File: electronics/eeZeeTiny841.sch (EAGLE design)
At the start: 12 parts, among them IC1 ATtiny841, J2 avrisp, Q1 16MHz

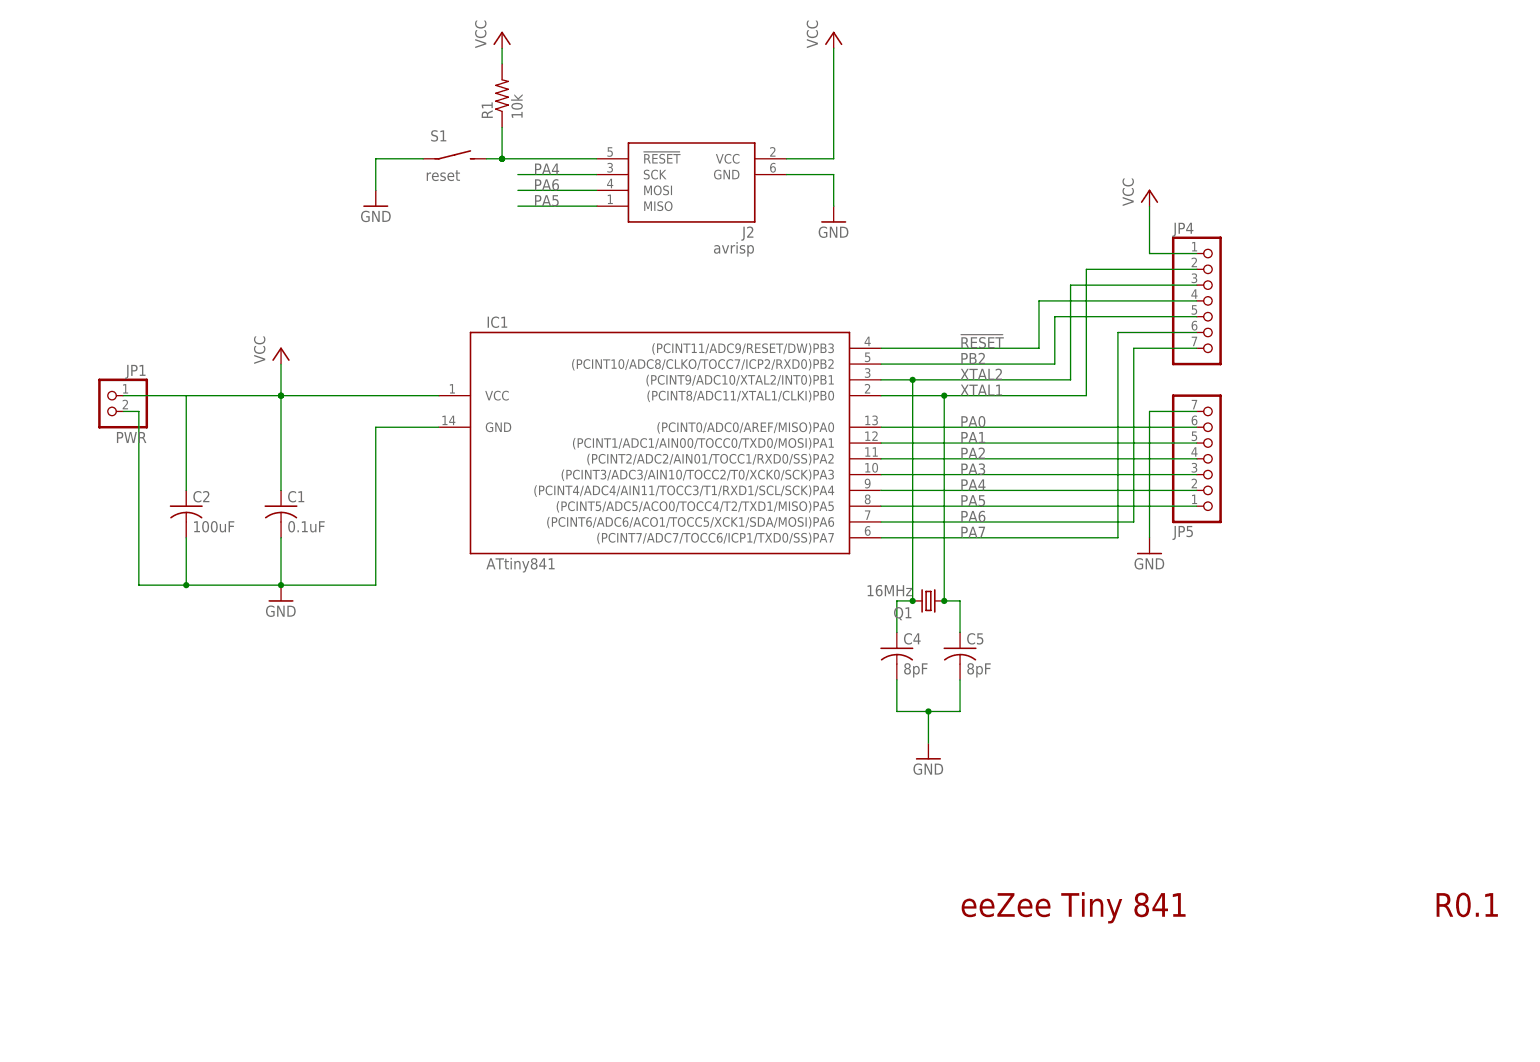
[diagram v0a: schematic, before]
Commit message: revised layout, updated logo
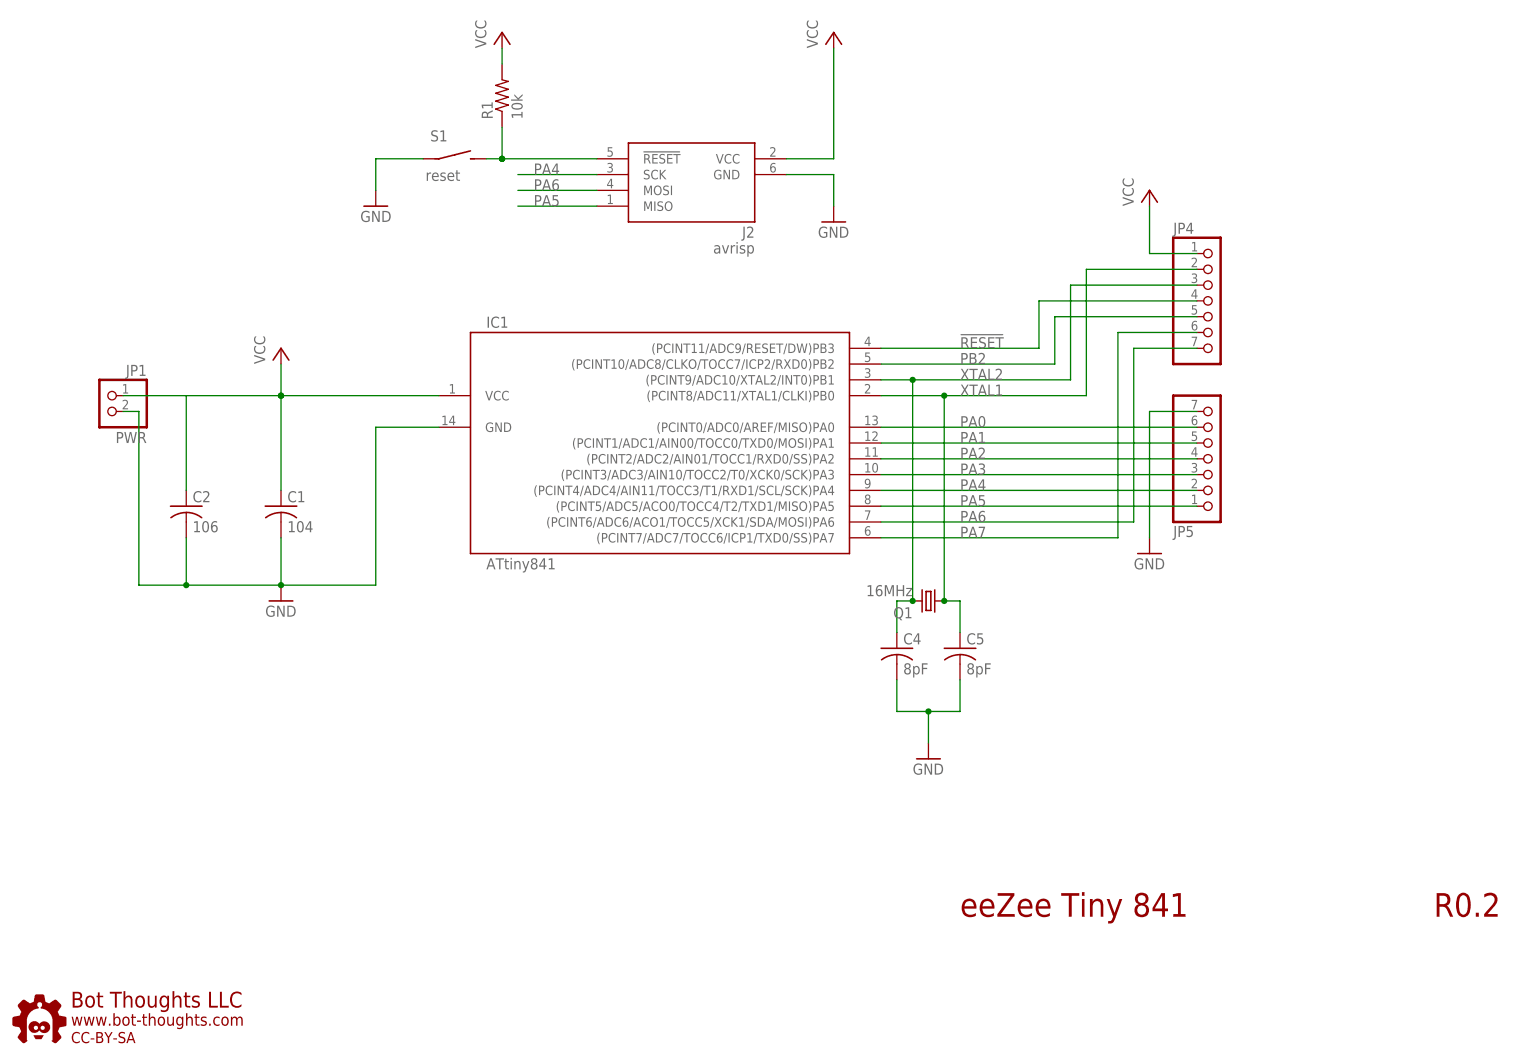
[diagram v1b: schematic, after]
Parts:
- added U$1: BTLOGO-LOGO-MD, bt:BTLOGO-LOGO-MD
- C1: value 0.1uF -> 104
- C2: value 100uF -> 106
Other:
- note added: "R0.2"
- note removed: "R0.1"
